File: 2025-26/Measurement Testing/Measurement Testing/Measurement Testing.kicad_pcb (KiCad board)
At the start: 2 copper layers, 21 parts, among them J1 Power Supply, J2 XT30PW-F, U1 TPS54308DDCR, U2 INA240A2PWR, U3 RASPBERRY_PI_PICO, U4 ADS8684IDBTR

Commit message: made pcb design
made a pcb design for the measurement board idk if its good we will go over it during meeting today i think. woaw :3
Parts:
- moved U3 66.7 mm to (129.5, 64.5), turned to -90 degrees
- moved C6 42.7 mm to (107.9, 78.2)
- moved J2 32.8 mm to (123.8, 91.5), turned to -90 degrees
- moved C2 28.2 mm to (111.7, 91.9)
- moved C3 27.8 mm to (107.5, 91.3), turned to 180 degrees
- moved C5 22.1 mm to (111.2, 78.5)
- moved J1 19.1 mm to (130.2, 93.0)
- moved R2 15.6 mm to (118.3, 88.5), turned to 90 degrees
- moved U2 15.3 mm to (115.8, 93.5), turned to 90 degrees
- moved Rshunt1 13.8 mm to (116.5, 99.5)
- moved U1 13.8 mm to (133.4, 79.9), turned to 90 degrees
- moved Cbst1 13.3 mm to (131.2, 78.4), turned to -90 degrees
- moved C1 12.1 mm to (108.2, 89.5), turned to 180 degrees
- moved U4 11.7 mm to (111.0, 84.0), turned to 90 degrees
- moved Cout1 11.1 mm to (133.7, 85.7), turned to 180 degrees
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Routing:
- net GND: track 0.00 -> 231.7 mm
- net /VIN: track 0.00 -> 66.3 mm
- net Net-(U3-GPIO19): track 0.00 -> 23.8 mm
- net Net-(J2-Pin_2): track 0.00 -> 16.8 mm
- net /5V_PSU/GND: track 0.00 -> 13.6 mm
- net /5V_PSU/Iout: track 0.00 -> 13.5 mm
- net Net-(U3-GPIO18): track 0.00 -> 11.4 mm
- net Net-(U3-GPIO16): track 0.00 -> 11.1 mm
- net Net-(U1-SW): track 0.00 -> 9.95 mm
- net Net-(U4-AIN_1P): track 0.00 -> 8.05 mm
- net Net-(U3-GPIO17): track 0.00 -> 7.24 mm
- net Net-(U1-FB): track 0.00 -> 5.01 mm
- net Net-(U4-REFCAP): track 0.00 -> 4.61 mm
- net Net-(U4-REFIO): track 0.00 -> 3.90 mm
- net Net-(U4-AIN_0P): track 0.00 -> 2.94 mm
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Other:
- board outline added: 58.1 x 53.1 mm

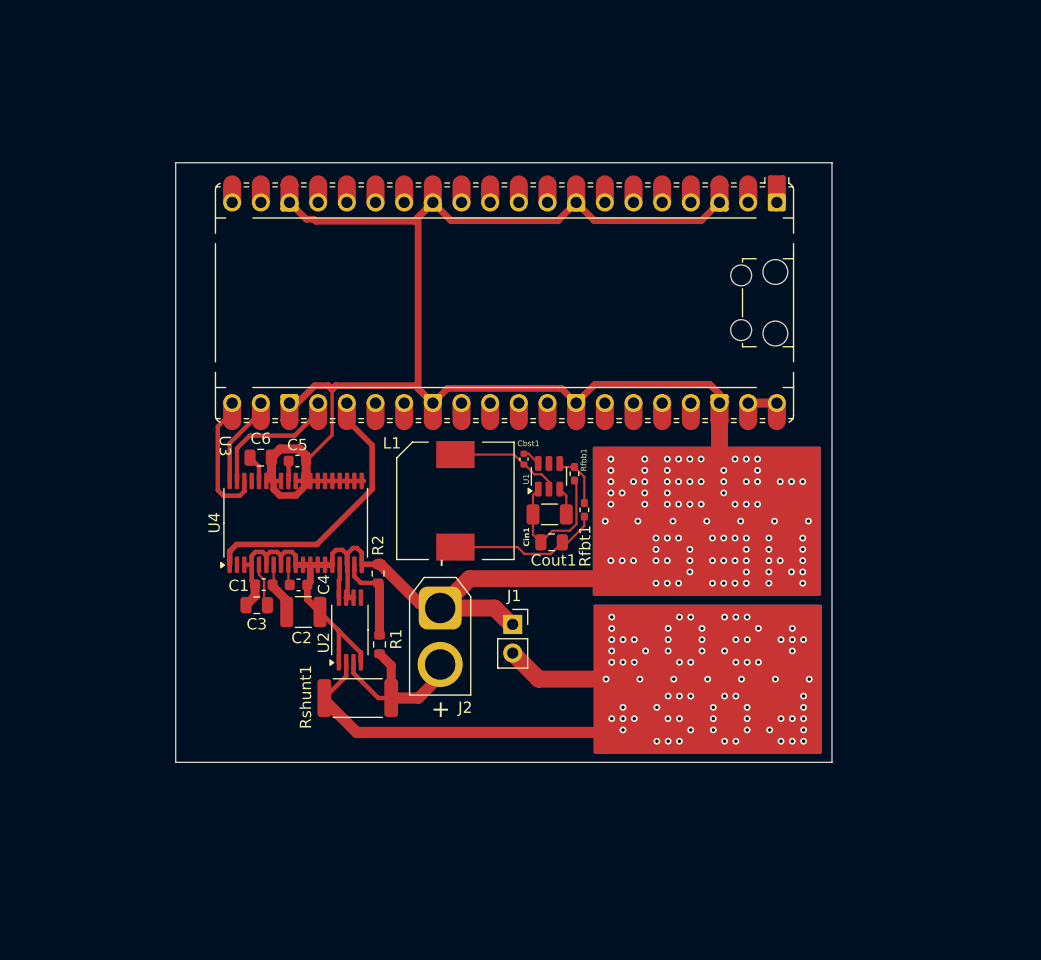
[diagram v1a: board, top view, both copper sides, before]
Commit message: fixed schem issues, reset my board bc it did not have a gnd plane
yahooooooooooo
fixed the labels to be global, fixed a missing ground on schem.
added a ground plane to the board, removed traces (to redo with the ground plane)
- Rowan :3
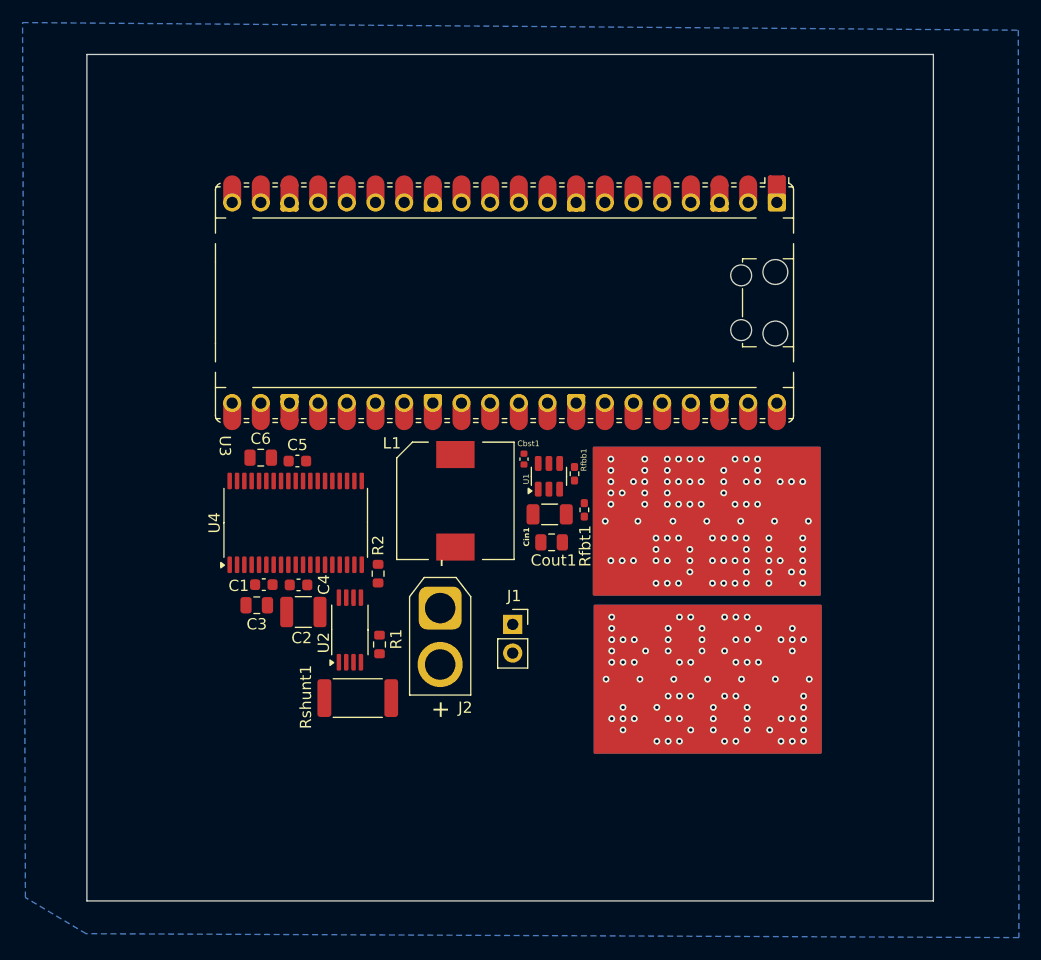
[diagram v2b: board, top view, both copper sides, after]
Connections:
- C4 pad 1: Net-(U4-AVDD) -> 5V
- C6 pad 1: Net-(U4-DVDD) -> 3V3
- Cin1 pad 2: /5V_PSU/GND -> GND
- Cout1 pad 2: /5V_PSU/GND -> GND
- Rfbb1 pad 2: /5V_PSU/GND -> GND
- U1 pad 1: /5V_PSU/GND -> GND
- U2 pad 5: unconnected-(U2-Pad5) -> 5V
- U3 pad 36: unconnected-(U3-3V3-Pad36) -> 3V3
- U3 pad 39: Net-(U3-VBUS) -> 5V
- U3 pad 40: Net-(U3-VBUS) -> 5V
- U4 pad 2: unconnected-(U4-~{RST}/~{PD}-Pad2) -> 3V3
- U4 pad 34: Net-(U4-DVDD) -> 3V3
- U4 pad 9: Net-(U4-AVDD) -> 5V
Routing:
- net GND: track 231.7 -> 0.00 mm
- net /VIN: track 66.3 -> 0.00 mm
- net Net-(U3-GPIO19): track 23.8 -> 0.00 mm
- net Net-(J2-Pin_2): track 16.8 -> 0.00 mm
- net /5V_PSU/GND: track 13.6 -> 0.00 mm
- net /5V_PSU/Iout: track 13.5 -> 0.00 mm
- net Net-(U3-GPIO18): track 11.4 -> 0.00 mm
- net Net-(U3-GPIO16): track 11.1 -> 0.00 mm
- net Net-(U1-SW): track 9.95 -> 0.00 mm
- net Net-(U4-AIN_1P): track 8.05 -> 0.00 mm
- net Net-(U3-GPIO17): track 7.24 -> 0.00 mm
- net Net-(U1-FB): track 5.01 -> 0.00 mm
- net Net-(U4-REFCAP): track 4.61 -> 0.00 mm
- net Net-(U4-REFIO): track 3.90 -> 0.00 mm
- net Net-(U4-AIN_0P): track 2.94 -> 0.00 mm
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- added copper zone on B.Cu, net GND
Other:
- board size 58.1 x 53.1 mm -> 75 x 75 mm

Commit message: basic layout done
yeah
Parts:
- L1, U3: moved to B.Cu
- moved Rshunt1 78.2 mm to (83.8, 28.5), turned to 180 degrees
- moved J2 76.8 mm to (73.5, 33.5), turned to 90 degrees
- moved R1 76.0 mm to (77.5, 30.7), turned to -90 degrees
- moved R2 68.2 mm to (77.5, 33.8), turned to -90 degrees
- moved U2 67.1 mm to (83.8, 34.5), turned to -90 degrees
- moved Cout1 66.0 mm to (91.0, 35.3), turned to -90 degrees
- moved Rfbt1 65.6 mm to (92.5, 34.2), turned to -90 degrees
- moved Rfbb1 61.1 mm to (92.5, 36.5)
- moved Cin1 59.3 mm to (98.5, 35.3), turned to -90 degrees
- moved U1 58.7 mm to (95.2, 35.3), turned to 180 degrees
- moved L1 55.6 mm to (95.0, 35.3), turned to 180 degrees
- moved Cbst1 55.0 mm to (94.2, 37.6), turned to 0 degrees
- moved C4 54.2 mm to (82.5, 43.5), turned to -90 degrees
- moved C5 53.6 mm to (71.0, 43.0), turned to 90 degrees
- moved U4 53.2 mm to (76.8, 43.2), turned to 180 degrees
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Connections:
- Cout1 pad 1: /5V_PSU/Iout -> 5V
- L1 pad 2: /5V_PSU/Iout -> 5V
- Rfbt1 pad 1: /5V_PSU/Iout -> 5V
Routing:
- net GND: track 0.00 -> 11.4 mm
- net Net-(U4-REFCAP): track 0.00 -> 6.81 mm
- net Net-(U4-REFIO): track 0.00 -> 2.78 mm
- net 5V: track 0.00 -> 2.49 mm
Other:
- board size 75 x 75 mm -> 60 x 50 mm

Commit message: mwahawhwhahwa i took over the branch and wired things up and also added miku the pcb should be finsisedh now maybe it can be checked woawawo
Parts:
- added G***: LOGO, Images:fish, F.Cu at (108.5, 49.0)
- added G***: LOGO, Images:snow_miku, F.Cu at (96.7, 45.0)
- moved Rfbb1 2.41 mm to (92.6, 34.1), turned to 90 degrees
- moved Rfbt1 2.10 mm to (92.6, 36.3), turned to 90 degrees
- moved C1 2.00 mm to (85.9, 46.2)
- moved C3 2.00 mm to (85.4, 48.7)
- moved C4 2.00 mm to (84.4, 44.2)
- moved C5 2.00 mm to (72.9, 43.7)
- moved C6 2.00 mm to (72.9, 47.2)
- moved U4 2.00 mm to (78.7, 44.0)
- moved C2 2.00 mm to (88.9, 47.2)
- moved U2 1.43 mm to (85.2, 34.5)
- moved Cbst1 0.38 mm to (94.6, 37.5)
- moved Cout1 0.15 mm to (91.1, 35.2), turned to 90 degrees
- moved U1 0.15 mm to (95.4, 35.2)
- moved Cin1 0.11 mm to (98.6, 35.4)
- moved L1 0.10 mm to (95.0, 35.2)
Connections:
- Cin1 pad 1: /5V_PSU/Vin -> VIN
- J1 pad 2: /VIN -> VIN
- Rshunt1 pad 1: /VIN -> VIN
- U1 pad 3: /5V_PSU/Vin -> VIN
- U2 pad 2: /VIN -> VIN
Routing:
- net 5V: track 2.49 -> 59.5 mm
- net 3V3: track 0.00 -> 41.4 mm
- net Net-(U4-AIN_1P): track 0.00 -> 12.1 mm
- net Net-(U3-GPIO18): track 0.00 -> 7.69 mm
- net Net-(U3-GPIO16): track 0.00 -> 7.01 mm
- net Net-(J2-Pin_2): track 0.00 -> 5.81 mm
- net Net-(U4-AIN_0P): track 0.00 -> 5.67 mm
- net Net-(U1-SW): track 0.00 -> 5.62 mm, vias 0 -> 2
- net GND: track 11.4 -> 16.8 mm, vias 89 -> 118
- net Net-(U3-GPIO19): track 0.00 -> 4.58 mm
- net Net-(U3-GPIO17): track 0.00 -> 4.50 mm
- net VIN: track 0.00 -> 3.68 mm, vias 0 -> 77
- net Net-(U1-FB): track 0.00 -> 2.85 mm
- net Net-(U4-AVDD__1): track 0.00 -> 2.13 mm
- net Net-(U1-BOOT): track 0.00 -> 0.96 mm
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
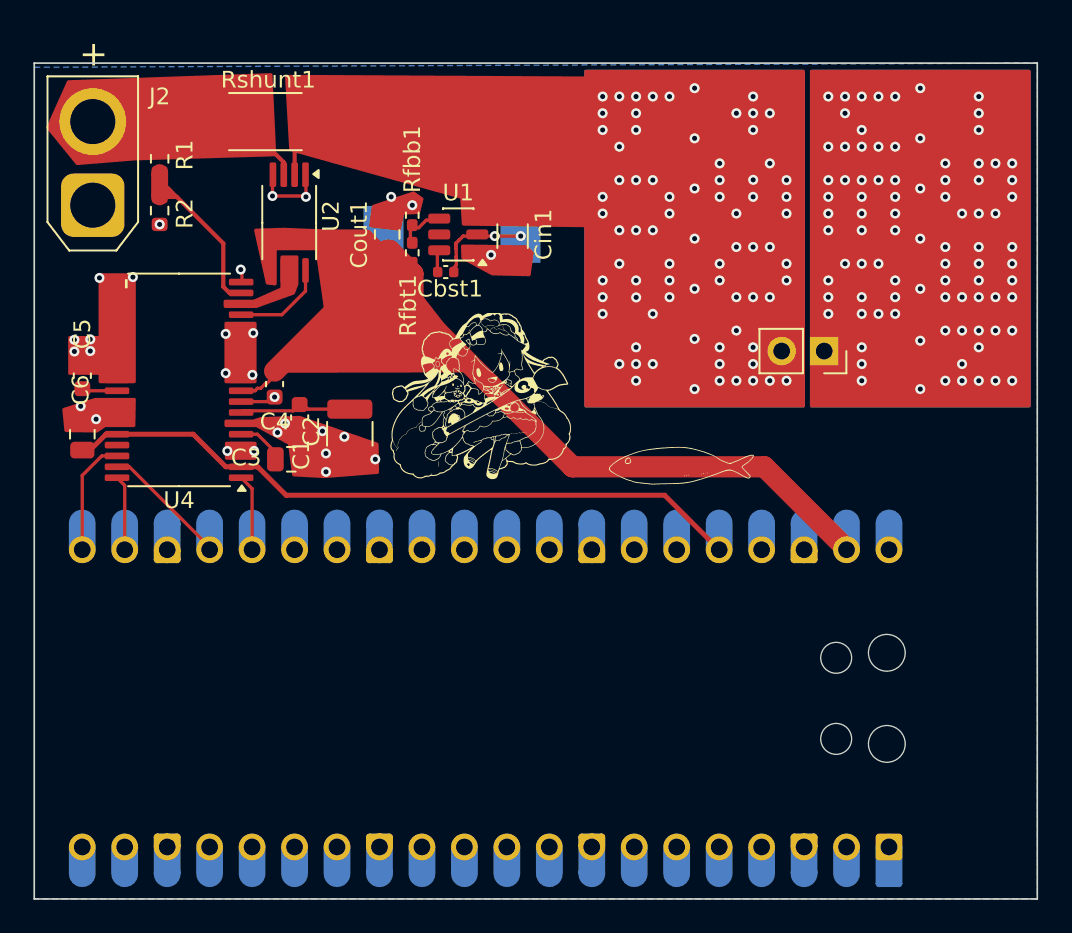
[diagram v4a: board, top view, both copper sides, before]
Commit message: addes second adc, compacted board, and redid traces
yippee
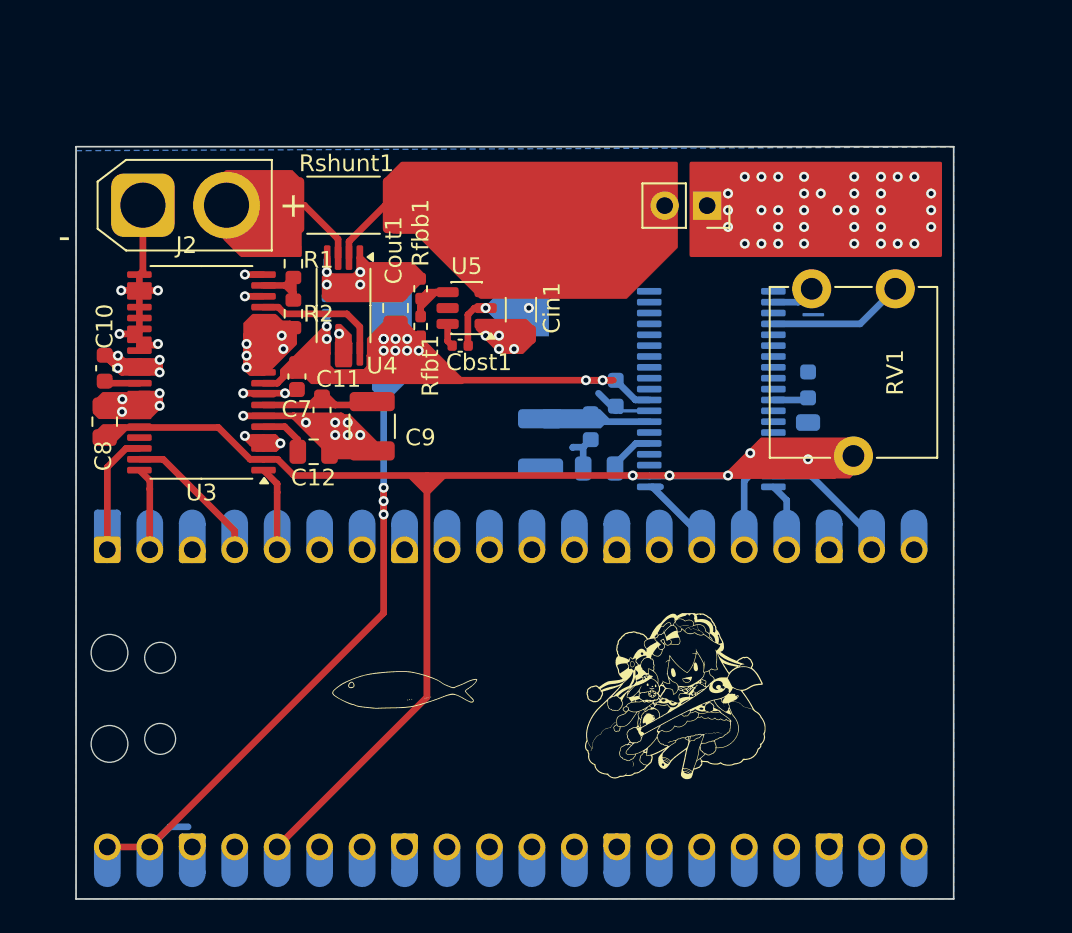
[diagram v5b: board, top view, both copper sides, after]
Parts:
- added C1: 10 uF, Capacitor_SMD:C_0805_2012Metric, B.Cu at (103.8, 49.2)
- added C2: 22 uF, Capacitor_SMD:C_1210_3225Metric, B.Cu at (100.3, 47.8)
- added C3: 1 uF, Capacitor_SMD:C_0603_1608Metric, B.Cu at (103.3, 46.8)
- added C4: 10 uF, Capacitor_SMD:C_0805_2012Metric, B.Cu at (116.3, 47.5)
- added C5: 1 uF, Capacitor_SMD:C_0603_1608Metric, B.Cu at (116.3, 44.2)
- added C6: 1 uF, Capacitor_SMD:C_0603_1608Metric, B.Cu at (104.8, 44.8)
- added Cbypass1: 100n, Capacitor_SMD:C_0402_1005Metric, B.Cu at (87.5, 39.5)
- added RV1: R_Potentiometer, Potentiometer_THT:Potentiometer_ACP_CA9-V10_Vertical, F.Cu at (116.5, 38.5)
- added U2: ADS8684IDBTR, Package_SO:TSSOP-38_6.1x12.5mm_P0.65mm, B.Cu at (110.5, 44.5)
- moved G*** 21.4 mm to (108.3, 62.9)
- moved G*** 21.3 mm to (92.0, 62.5)
- moved J1 11.2 mm to (110.2, 33.5)
- moved R1 10.2 mm to (85.5, 37.0)
- moved R2 10.1 mm to (85.5, 40.0)
- moved Rshunt1 6.85 mm to (88.5, 33.5)
- moved U4 5.93 mm to (88.5, 39.5)
- moved Cbst1 4.49 mm to (95.5, 41.9)
- moved Cout1 4.43 mm to (91.6, 39.7)
- moved L1 4.43 mm to (95.5, 39.6)
- moved Rfbb1 4.43 mm to (93.1, 38.5)
- moved Rfbt1 4.43 mm to (93.1, 40.8)
- moved U5 4.43 mm to (95.9, 39.7)
- moved Cin1 4.43 mm to (99.1, 39.8)
- moved J2 3.00 mm to (76.5, 33.5), turned to 0 degrees
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- renumbered C5 to C10, C1 to C11, C3 to C12, C4 to C7, C6 to C8, C2 to C9, U3 to U1, U4 to U3, U2 to U4, U1 to U5
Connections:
- U1 pad 1: unconnected-(U3-GPIO0-Pad1) -> Net-(U1-GPIO0)
- U1 pad 15: unconnected-(U3-GPIO11-Pad15) -> Net-(U1-GPIO11)
- U1 pad 16: unconnected-(U3-GPIO12-Pad16) -> Net-(U1-GPIO12)
- U1 pad 17: unconnected-(U3-GPIO13-Pad17) -> Net-(U1-GPIO13)
- U1 pad 19: unconnected-(U3-GPIO14-Pad19) -> Net-(U1-GPIO14)
- U1 pad 2: unconnected-(U3-GPIO1-Pad2) -> Net-(U1-GPIO1)
- U1 pad 21: Net-(U3-GPIO16) -> unconnected-(U1-GPIO16-Pad21)
- U1 pad 22: Net-(U3-GPIO17) -> unconnected-(U1-GPIO17-Pad22)
- U1 pad 24: Net-(U3-GPIO18) -> unconnected-(U1-GPIO18-Pad24)
- U1 pad 25: Net-(U3-GPIO19) -> unconnected-(U1-GPIO19-Pad25)
- U1 pad 4: unconnected-(U3-GPIO2-Pad4) -> Net-(U1-GPIO2)
- U1 pad 5: unconnected-(U3-GPIO3-Pad5) -> Net-(U1-GPIO3)
- U3 pad 1: Net-(U3-GPIO19) -> Net-(U1-GPIO3)
- U3 pad 36: Net-(U3-GPIO16) -> Net-(U1-GPIO0)
- U3 pad 37: Net-(U3-GPIO18) -> Net-(U1-GPIO2)
- U3 pad 38: Net-(U3-GPIO17) -> Net-(U1-GPIO1)
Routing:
- net GND: track 16.8 -> 97.7 mm, vias 118 -> 75
- net 3V3: track 41.4 -> 92.1 mm, vias 0 -> 5
- net 5V: track 59.5 -> 86.5 mm, vias 0 -> 15
- net VIN: track 3.68 -> 30.1 mm, vias 77 -> 0
- net Net-(U2-REFCAP): track 0.00 -> 15.1 mm
- net Net-(U1-GPIO2): track 0.00 -> 8.61 mm
- net Net-(U2-AIN_3P): track 0.00 -> 8.16 mm
- net Net-(U3-AIN_1P): track 12.1 -> 4.41 mm
- net Net-(U3-GPIO18): track 7.69 -> 0.00 mm
- net Net-(U1-GPIO14): track 0.00 -> 7.37 mm
- net Net-(U1-GPIO0): track 0.00 -> 7.32 mm
- net Net-(U5-SW): track 5.62 -> 12.9 mm
- net Net-(U3-GPIO16): track 7.01 -> 0.00 mm
- net Net-(J2-Pin_2): track 5.81 -> 11.3 mm
- net Net-(U1-GPIO12): track 0.00 -> 5.45 mm
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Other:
- board size 60 x 50 mm -> 52.5 x 45 mm
- board text added: "PICO ON THIS SIDE!"
- board text added: "port that way ->"

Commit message: trying to panelize before ordering
i have no clue what kikit does
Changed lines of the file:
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@@
 		)
 		(fp_text user "-"
-			(at -4.7 1.875 0)
+			(at -2.2 2.9 0)
 			(layer "F.SilkS")
 			(effects
@@
 	(gr_poly
 		(pts
-			(xy 90.3 40.9) (xy 90.3 44.5) (xy 91 45.2) (xy 91 45.2) (xy 93.9 42.3) (xy 92.5 40.9)
+			(xy 90.3 40.9) (xy 90.3 44.5) (xy 91 45.2) (xy 93.9 42.3) (xy 92.5 40.9)
 		)
 		(stroke

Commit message: a lot has been done
i dont even remember
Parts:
- U2, U3: footprint Package_SO:TSSOP-38_6.1x12.5mm_P0.65mm -> Package_SO:TSSOP-38_4.4x9.7mm_P0.5mm
- moved RV1 12.5 mm to (123.0, 49.2), turned to 90 degrees
- moved C4 0.50 mm to (116.3, 47.0), turned to 0 degrees
- moved R2 0.50 mm to (85.5, 40.5)
- moved Cbst1 0.16 mm to (95.3, 41.9)
- moved Cout1 0.16 mm to (91.5, 39.7)
- moved Rfbb1 0.16 mm to (93.0, 38.5)
- moved Rfbt1 0.16 mm to (93.0, 40.8)
- moved U5 0.16 mm to (95.7, 39.7)
- moved C9 0.12 mm to (90.2, 46.6)
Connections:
- RV1 pad 1: Net-(U2-AIN_2P) -> GND
- RV1 pad 2: 3V3 -> Net-(U2-AIN_2P)
- RV1 pad 3: Net-(U2-AIN_3P) -> 3V3
- U2 pad 23: Net-(U2-AIN_3P) -> GND
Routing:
- net GND: track 97.7 -> 143.7 mm, vias 75 -> 77
- net Net-(U2-AIN_3P): track 8.16 -> 0.00 mm
- net 5V: track 86.5 -> 94.3 mm, vias 15 -> 17
- net Net-(U2-REFCAP): track 15.1 -> 7.51 mm
- net Net-(J2-Pin_2): track 11.3 -> 4.59 mm
- net Net-(U5-SW): track 12.9 -> 6.19 mm
- net Net-(U2-AIN_2P): track 2.62 -> 7.68 mm
- net 3V3: track 92.1 -> 88.0 mm, vias 5 -> 6
- net VIN: track 30.1 -> 27.6 mm
- net Net-(U1-GPIO12): track 5.45 -> 7.43 mm
- net Net-(U1-GPIO13): track 3.29 -> 4.99 mm
- net Net-(U1-GPIO3): track 5.10 -> 6.80 mm
- net Net-(U3-AIN_1P): track 4.41 -> 2.77 mm
- net Net-(U1-GPIO0): track 7.32 -> 8.81 mm
- net Net-(U1-GPIO14): track 7.37 -> 8.72 mm
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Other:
- board text added: "U3"
